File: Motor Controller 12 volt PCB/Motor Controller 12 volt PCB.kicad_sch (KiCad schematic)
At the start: 7 parts, among them J2 776279-1, K1 PR22-12V-400-1A

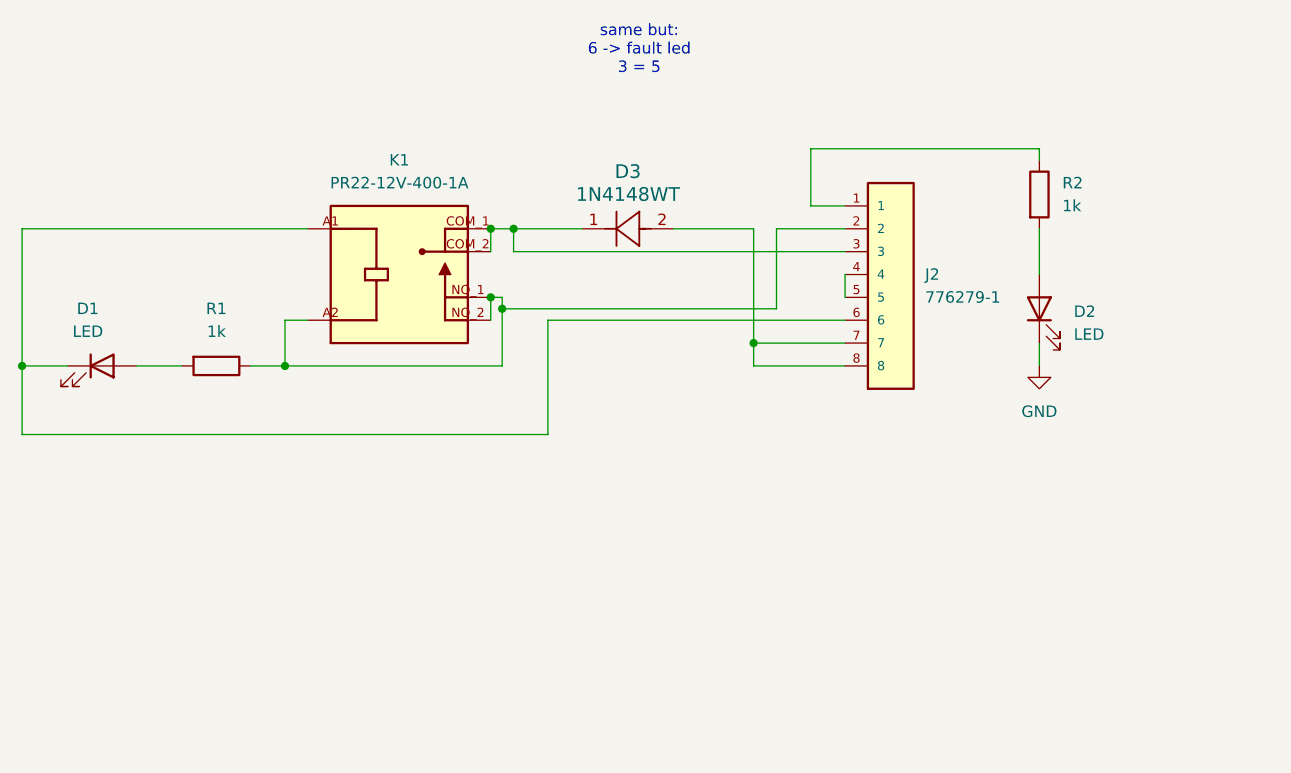
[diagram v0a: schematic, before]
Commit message: 12 v power supply pcb with mounting holes
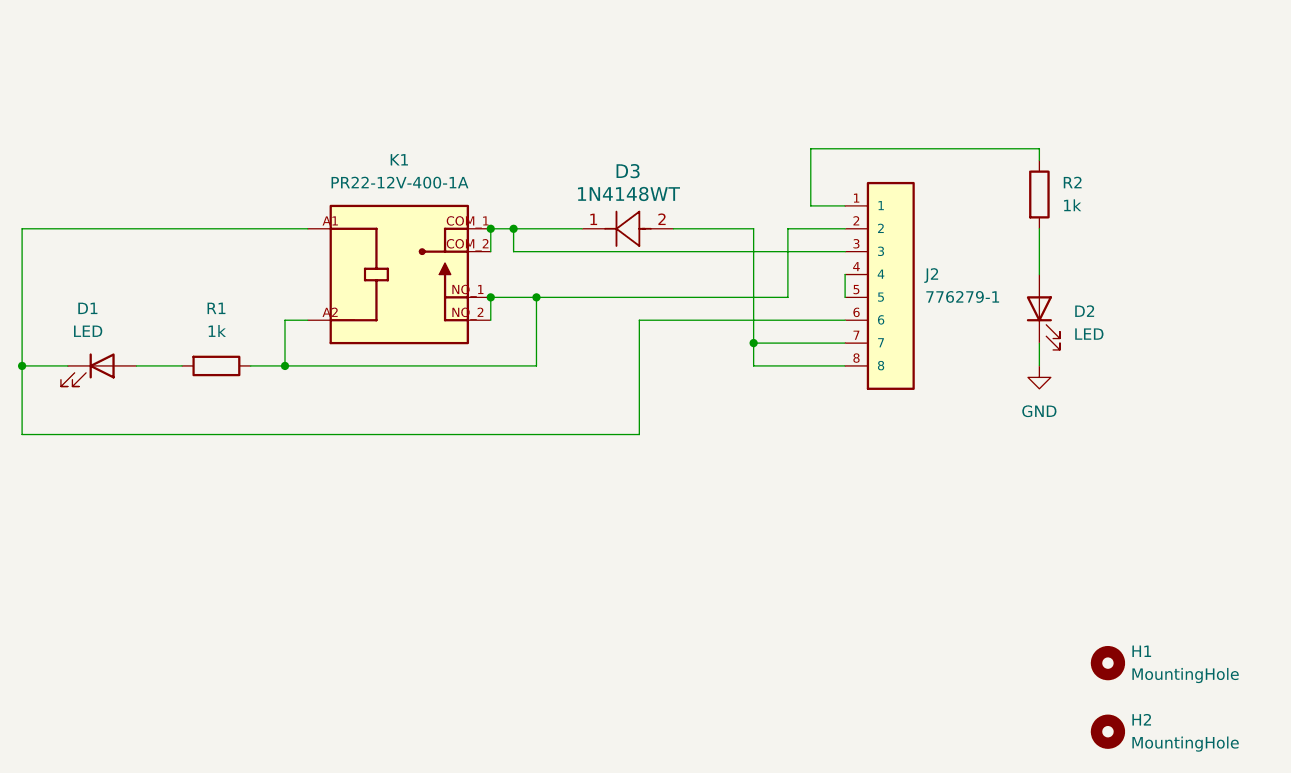
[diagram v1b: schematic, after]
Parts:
- added H1, H2: MountingHole, MountingHole:MountingHole_3.2mm_M3, symbol Mechanical:MountingHole
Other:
- note removed: "same but: 6 -> fault led 3 = 5"
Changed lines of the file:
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@@
 	(generator_version "9.0")
 	(paper "A4")
-	(text "same but:\n6 -> fault led\n3 = 5"
-		(exclude_from_sim no)
-		(at 161.29 58.928 0)
-		(effects
-			(font
-				(size 1.27 1.27)
-			)
-		)
-	)
-	(junction
-		(at 146.05 87.63)
-		(diameter 0)
-		(color 0 0 0 0)
-	)
 	(junction
 		(at 147.32 78.74)
@@
 	)
 	(junction
+		(at 149.86 86.36)
+		(diameter 0)
+		(color 0 0 0 0)
+	)
+	(junction
 		(at 144.78 86.36)
 		(diameter 0)
@@
 	(wire
 		(pts
-			(xy 146.05 86.36) (xy 144.78 86.36)
-		)
-		(stroke
-			(width 0)
-			(type default)
-		)
-	)
-	(wire
-		(pts
-			(xy 184.15 78.74) (xy 176.53 78.74)
+			(xy 144.78 86.36) (xy 149.86 86.36)
+		)
+		(stroke
+			(width 0)
+			(type default)
+		)
+	)
+	(wire
+		(pts
+			(xy 184.15 78.74) (xy 177.8 78.74)
 		)
 		(stroke
@@
 	(wire
 		(pts
-			(xy 176.53 78.74) (xy 176.53 87.63)
-		)
-		(stroke
-			(width 0)
-			(type default)
-		)
-	)
-	(wire
-		(pts
-			(xy 146.05 87.63) (xy 146.05 93.98)
-		)
-		(stroke
-			(width 0)
-			(type default)
-		)
-	)
-	(wire
-		(pts
-			(xy 121.92 93.98) (xy 146.05 93.98)
+			(xy 177.8 78.74) (xy 177.8 86.36)
+		)
+		(stroke
+			(width 0)
+			(type default)
+		)
+	)
+	(wire
+		(pts
+			(xy 121.92 93.98) (xy 149.86 93.98)
 		)
 		(stroke
@@
 	(wire
 		(pts
-			(xy 146.05 86.36) (xy 146.05 87.63)
-		)
-		(stroke
-			(width 0)
-			(type default)
-		)
-	)
-	(wire
-		(pts
 			(xy 180.34 69.85) (xy 205.74 69.85)
 		)
@@
 	(wire
 		(pts
-			(xy 92.71 101.6) (xy 151.13 101.6)
+			(xy 92.71 101.6) (xy 161.29 101.6)
 		)
 		(stroke
@@
 	(wire
 		(pts
-			(xy 151.13 88.9) (xy 184.15 88.9)
+			(xy 161.29 88.9) (xy 184.15 88.9)
 		)
 		(stroke
@@
 	(wire
 		(pts
-			(xy 151.13 101.6) (xy 151.13 88.9)
-		)
-		(stroke
-			(width 0)
-			(type default)
-		)
-	)
-	(wire
-		(pts
-			(xy 176.53 87.63) (xy 146.05 87.63)
+			(xy 149.86 86.36) (xy 149.86 93.98)
+		)
+		(stroke
+			(width 0)
+			(type default)
+		)
+	)
+	(wire
+		(pts
+			(xy 161.29 101.6) (xy 161.29 88.9)
+		)
+		(stroke
+			(width 0)
+			(type default)
+		)
+	)
+	(wire
+		(pts
+			(xy 177.8 86.36) (xy 149.86 86.36)
 		)
 		(stroke
@@
 					(unit 1)
 				)
+			)
+		)
+	)
+	(symbol
+		(lib_id "Mechanical:MountingHole")
+		(at 213.36 127 0)
+		(unit 1)
+		(exclude_from_sim no)
+		(in_bom no)
+		(on_board yes)
+		(dnp no)
+		(fields_autoplaced yes)
+		(property "Reference" "H1"
+			(at 215.9 125.7299 0)
+			(effects
+				(font
+					(size 1.27 1.27)
+				)
+				(justify left)
+			)
+		)
+		(property "Value" "MountingHole"
+			(at 215.9 128.2699 0)
+			(effects
+				(font
+					(size 1.27 1.27)
+				)
+				(justify left)
+			)
+		)
+		(property "Footprint" "MountingHole:MountingHole_3.2mm_M3"
+			(at 213.36 127 0)
+			(effects
+				(font
+					(size 1.27 1.27)
+				)
+				(hide yes)
+			)
+		)
+		(property "Datasheet" "~"
+			(at 213.36 127 0)
+			(effects
+				(font
+					(size 1.27 1.27)
+				)
+				(hide yes)
+			)
+		)
+		(property "Description" "Mounting Hole without connection"
+			(at 213.36 127 0)
+			(effects
+				(font
+					(size 1.27 1.27)
+				)
+				(hide yes)
+			)
+		)
+		(instances
+			(project ""
+				(path "/42681819-136d-4d5a-bbbe-1c47b8dad30e"
+					(reference "H1")
+					(unit 1)
+				)
+			)
+		)
+	)
+	(symbol
+		(lib_id "Mechanical:MountingHole")
+		(at 213.36 134.62 0)
+		(unit 1)
+		(exclude_from_sim no)
+		(in_bom no)
+		(on_board yes)
+		(dnp no)
+		(fields_autoplaced yes)
+		(property "Reference" "H2"
+			(at 215.9 133.3499 0)
+			(effects
+				(font
+					(size 1.27 1.27)
+				)
+				(justify left)
+			)
+		)
+		(property "Value" "MountingHole"
+			(at 215.9 135.8899 0)
+			(effects
+				(font
+					(size 1.27 1.27)
+				)
+				(justify left)
+			)
+		)
+		(property "Footprint" "MountingHole:MountingHole_3.2mm_M3"
+			(at 213.36 134.62 0)
+			(effects
+				(font
+					(size 1.27 1.27)
+				)
+				(hide yes)
+			)
+		)
+		(property "Datasheet" "~"
+			(at 213.36 134.62 0)
+			(effects
+				(font
+					(size 1.27 1.27)
+				)
+				(hide yes)
+			)
+		)
+		(property "Description" "Mounting Hole without connection"
+			(at 213.36 134.62 0)
+			(effects
+				(font
+					(size 1.27 1.27)
+				)
+				(hide yes)
+			)
+		)
+		(instances
+			(project ""
+				(path "/42681819-136d-4d5a-bbbe-1c47b8dad30e"
+					(reference "H2")
+					(unit 1)
+				)
